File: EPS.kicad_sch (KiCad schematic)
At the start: 41 parts, among them SW101 Deploy, SW102 Deploy, SW103 Deploy

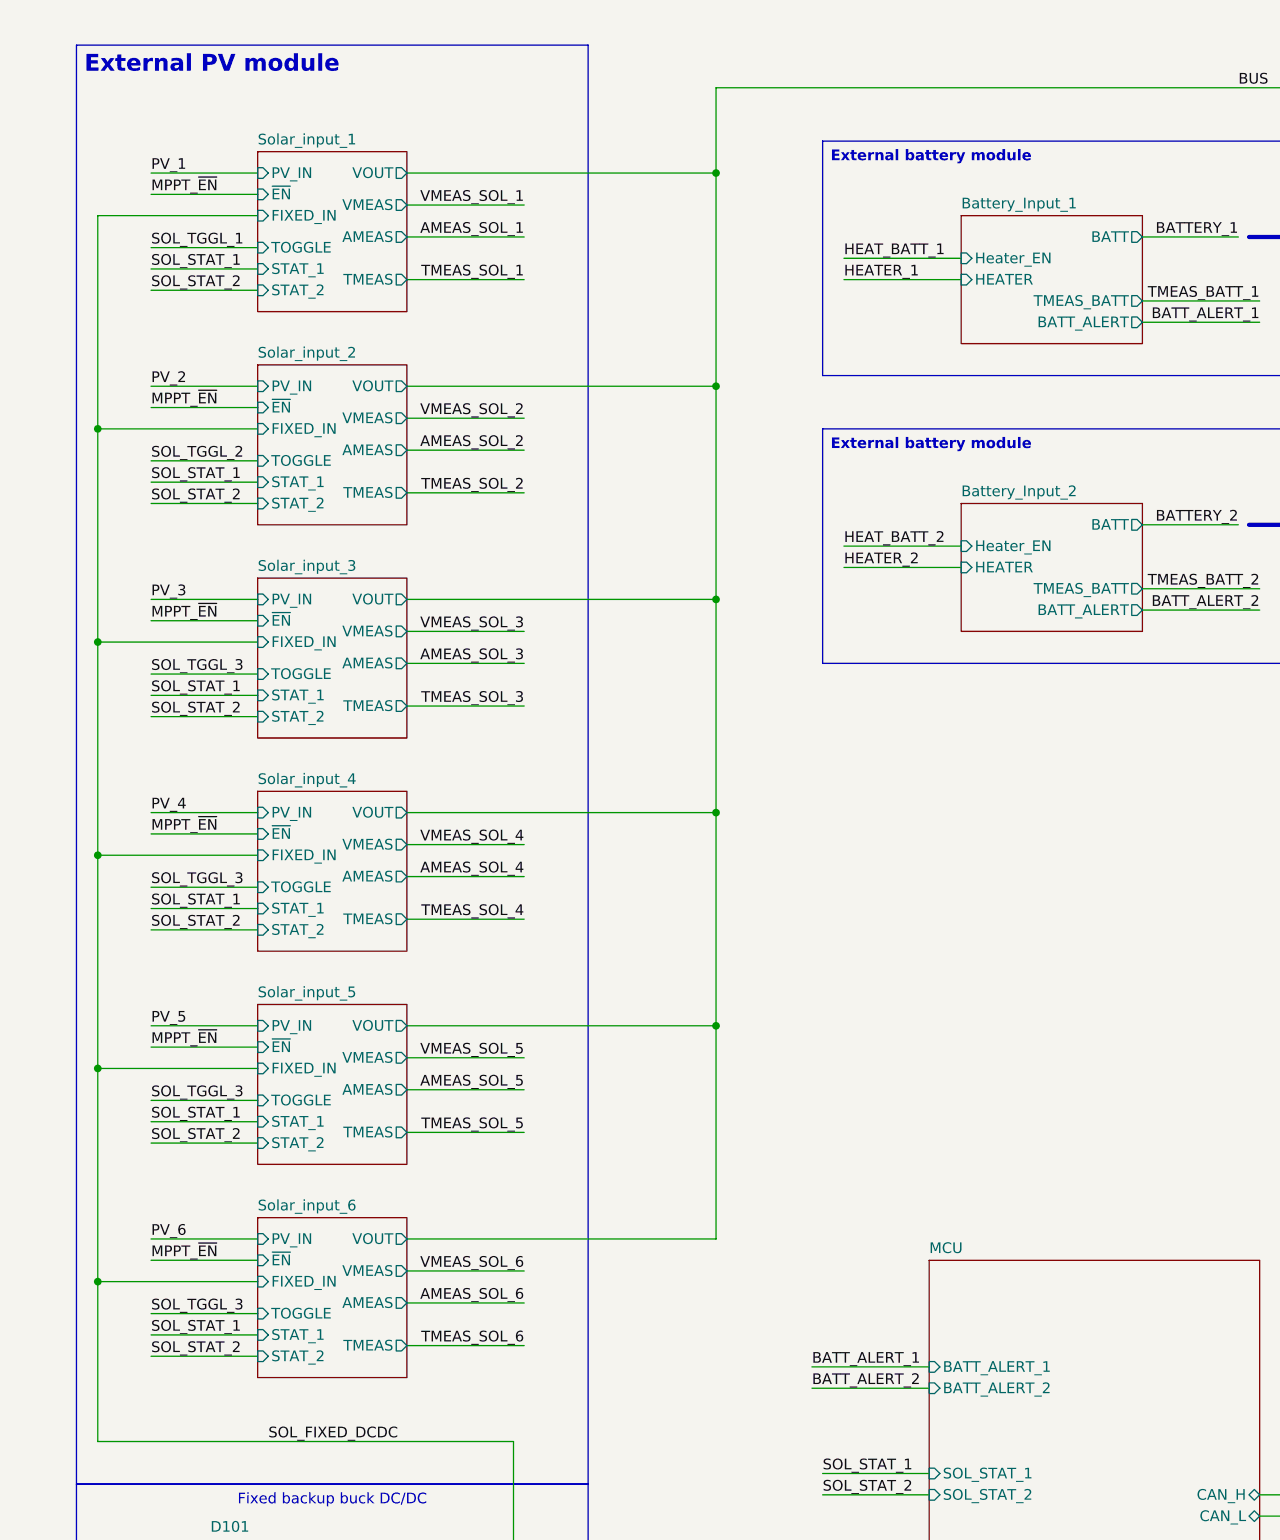
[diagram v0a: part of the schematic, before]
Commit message: replaced individual CC sourses for SOL with a single one
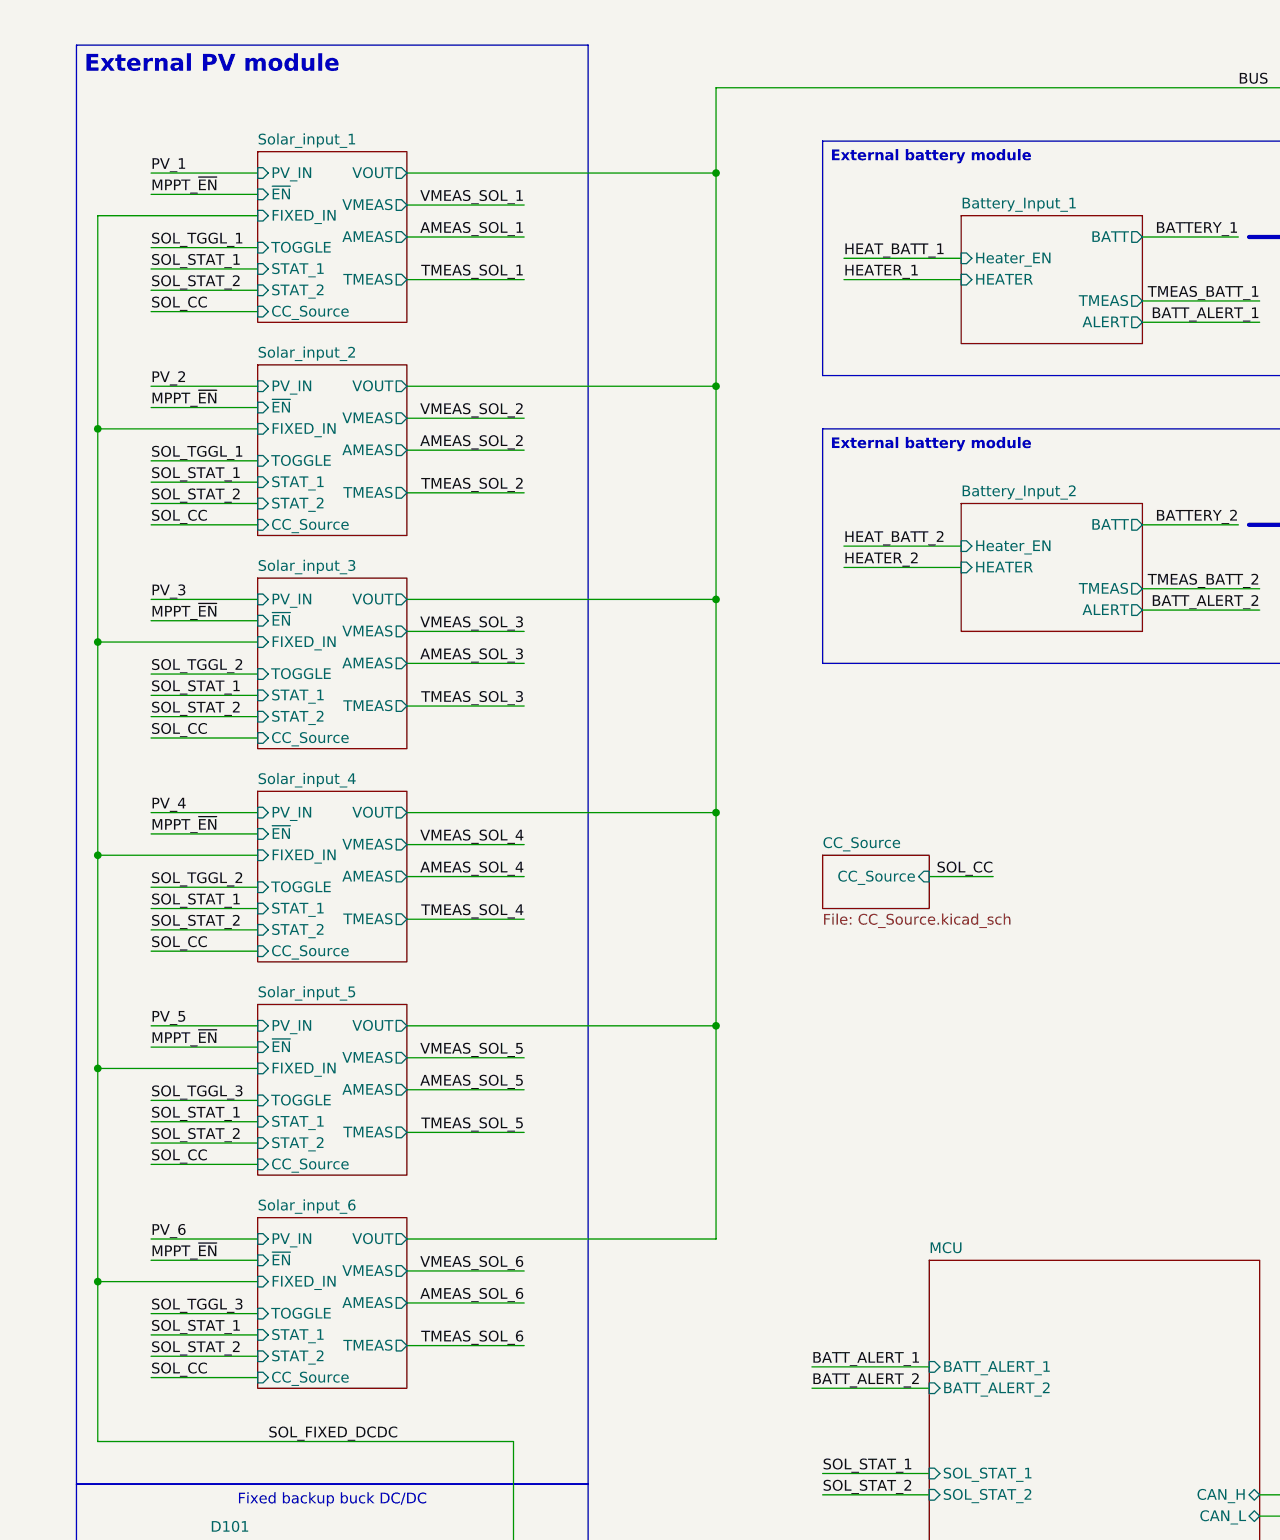
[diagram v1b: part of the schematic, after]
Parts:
- SW101, SW102, SW103: footprint (none) -> Connector_PinSocket_2.54mm:PinSocket_1x02_P2.54mm_Vertical
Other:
- added sheet CC_Source (CC_Source.kicad_sch)
- sheet Battery_Input_1 ports: added ALERT, TMEAS; removed BATT_ALERT, TMEAS_BATT
- sheet Battery_Input_2 ports: added ALERT, TMEAS; removed BATT_ALERT, TMEAS_BATT
- sheet Solar_input_1 ports: added CC_Source; removed none
- sheet Solar_input_2 ports: added CC_Source; removed none
- sheet Solar_input_3 ports: added CC_Source; removed none
- sheet Solar_input_4 ports: added CC_Source; removed none
- sheet Solar_input_5 ports: added CC_Source; removed none
- sheet Solar_input_6 ports: added CC_Source; removed none

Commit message: restructurization of the entire project improved
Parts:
- removed C101: 1n, Capacitor_SMD:C_0805_2012Metric_Pad1.18x1.45mm_HandSolder, symbol Device:C_Small
- removed D101, D102, D103, D104, D105, D106: D_Schottky, Diode_SMD:D_0805_2012Metric, symbol Device:D_Schottky
- removed FID101, FID102, FID103, FID104, FID105, FID106, FID107, FID108: Fiducial, Fiducial:Fiducial_1mm_Mask2mm, symbol Mechanical:Fiducial
- removed H101, H102, H103, H104, H105, H106, H107, H108, H109, H110, H111, H112, H113, H114, H115, H116: MountingHole, MountingHole:MountingHole_3.2mm_M3_Pad_Via, symbol Mechanical:MountingHole_Pad
- removed PCB101, PCB102, PCB103, PCB104: PCB Outline, Outlines:SPACEMANIC_V1c, symbol Mechanical:MountingHole
- removed R101, R102: 1M, Resistor_SMD:R_0603_1608Metric_Pad0.98x0.95mm_HandSolder, symbol Device:R_Small
- removed R103: TBD, Resistor_SMD:R_0603_1608Metric_Pad0.98x0.95mm_HandSolder, symbol Device:R_Small
- removed SW101, SW102, SW103: Deploy, Connector_PinSocket_2.54mm:PinSocket_1x02_P2.54mm_Vertical, symbol Switch:SW_Push
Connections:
- no-connect marks 3 -> 0
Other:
- removed sheet 5V_DCDC_1
- removed sheet AMEAS_BATT_1
- removed sheet AMEAS_BUS
- removed sheet AMEAS__BATT_2
- removed sheet Battery_Input_1
- removed sheet Battery_Input_2
- removed sheet CC_Source
- removed sheet Channel_Matrix
- removed sheet Interface
- removed sheet MCU
- removed sheet Solar_input_1
- removed sheet Solar_input_2
- removed sheet Solar_input_3
- removed sheet Solar_input_4
- removed sheet Solar_input_5
- removed sheet Solar_input_6
- removed sheet Switch_BATT_1
- removed sheet Switch_BATT_2
- removed sheet Switch_Deploy_BUS
- added sheet BATTERY (EPS_BATTERY_PACK/EPS_BATTERY_PACK.kicad_sch)
- added sheet CORE (EPS_CORE/EPS_CORE.kicad_sch)
- added sheet OUTPUT_CHANNELS (EPS_OUTPUT_CHANNELS/EPS_OUTPUT_CHANNELS.kicad_sch)
- added sheet PV_INPUT (EPS_PV_INPUT/EPS_PV_INPUT.kicad_sch)
- note added: "ANALOG"
- note added: "DIGITAL"
- note added: "ENABLES"
- note added: "FEEDBACK"
- note added: "KILL SWITCH"
- note added: "MAIN SIGNAL BUS"
- note added: "POWER"
- note added: "POWER CONN"
- note added: "SIGNAL BUS"
- note added: "T MEAS"
- note added: "VA MEAS"
- note added: "i2C"
- note removed: "Connector"
- note removed: "MAIN SWITCH"
- note removed: "Shared backup DCDC to save space"
